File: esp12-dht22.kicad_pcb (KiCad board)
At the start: 2 copper layers, 42.9 x 18.5 mm, 12 parts, among them J1 Battery, U1 ESP-12E, U2 DHT22

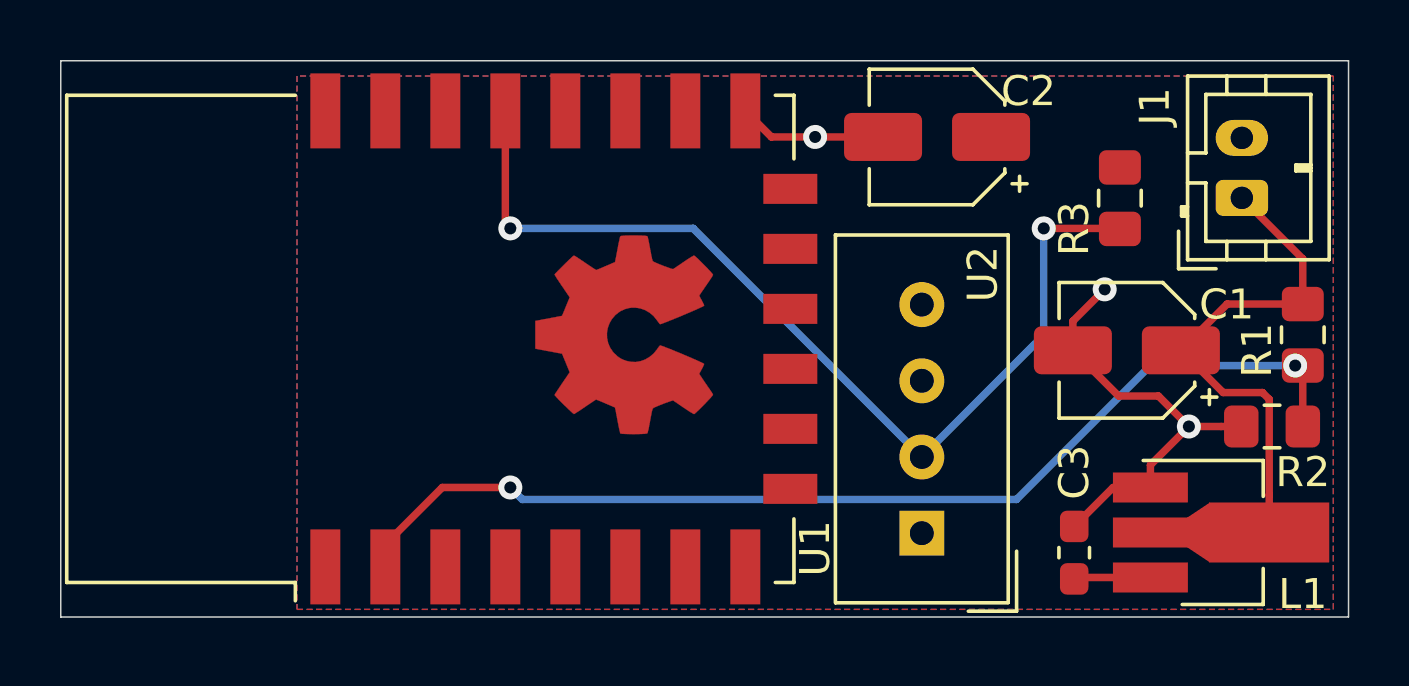
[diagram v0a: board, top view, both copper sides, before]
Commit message: added connection between RST and GPIO16 for wakeup from deep sleep fixes #1
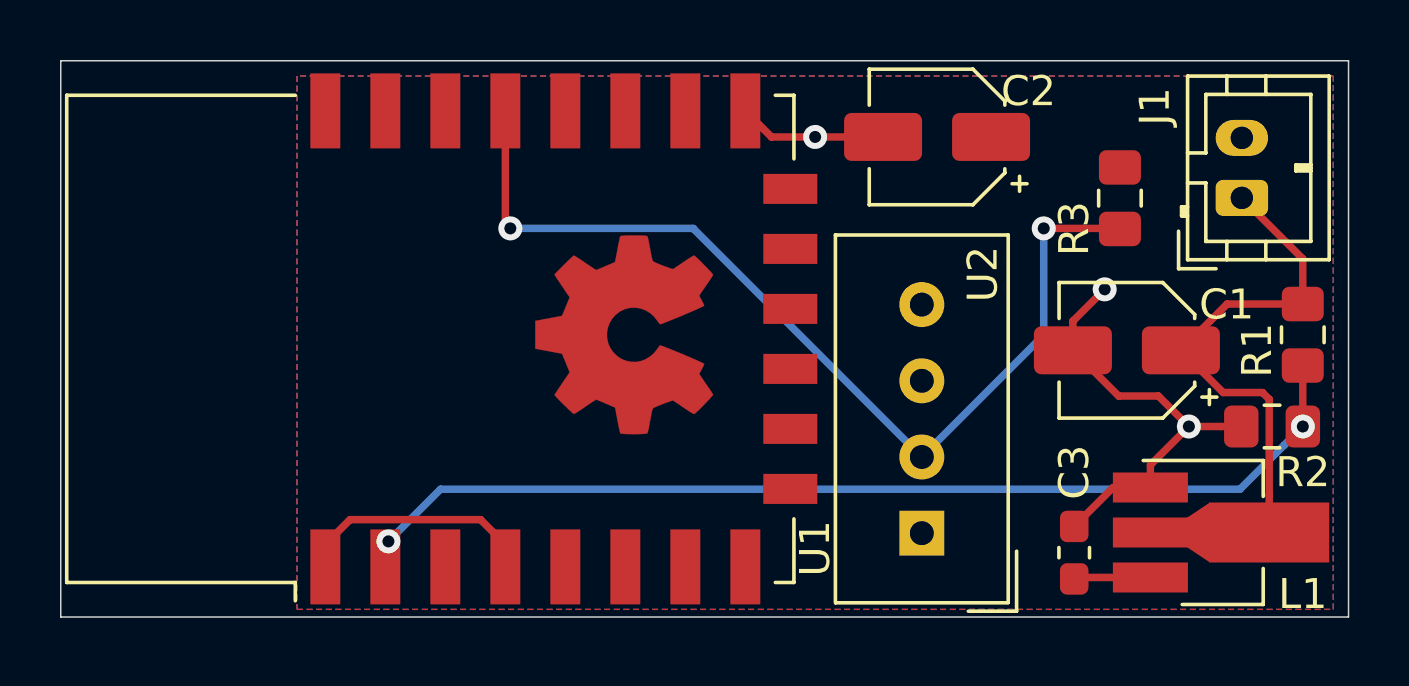
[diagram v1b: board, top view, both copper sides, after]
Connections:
- U1 pad 1: Net-(U1-Pad1) -> DeepSleep
- U1 pad 4: Net-(U1-Pad4) -> DeepSleep
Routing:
- net DeepSleep: track 0.00 -> 8.18 mm
- net ADC: track 36.2 -> 35.0 mm

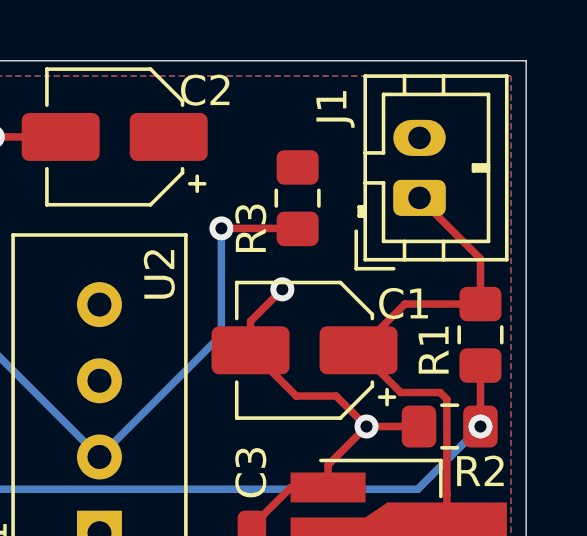
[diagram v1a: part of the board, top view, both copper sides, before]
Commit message: swapped pins of J1 fixes #4
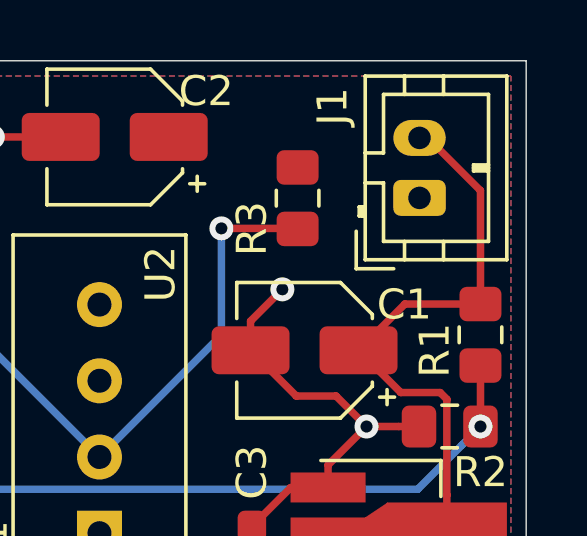
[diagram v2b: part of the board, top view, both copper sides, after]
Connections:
- J1 pad 1: +BATT -> GND
- J1 pad 2: GND -> +BATT
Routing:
- net +BATT: track 21.1 -> 23.3 mm
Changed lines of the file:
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@@
-(kicad_pcb (version 20171130) (host pcbnew 5.1.2-f72e74a~84~ubuntu18.10.1)
+(kicad_pcb (version 20171130) (host pcbnew 5.1.3-ffb9f22~84~ubuntu18.10.1)
   (general
     (thickness 1.6)
     (drawings 7)
-    (tracks 54)
+    (tracks 55)
     (zones 0)
     (modules 12)
@@
     )
     (pad 1 thru_hole roundrect (at 0 0 90) (size 1.2 1.75) (drill 0.75) (layers *.Cu *.Mask) (roundrect_rratio 0.208333)
+      (net 1 GND))
+    (pad 2 thru_hole oval (at 2 0 90) (size 1.2 1.75) (drill 0.75) (layers *.Cu *.Mask)
       (net 2 +BATT))
-    (pad 2 thru_hole oval (at 2 0 90) (size 1.2 1.75) (drill 0.75) (layers *.Cu *.Mask)
-      (net 1 GND))
     (model ${KISYS3DMOD}/Connector_JST.3dshapes/JST_PH_B2B-PH-K_1x02_P2.00mm_Vertical.wrl
       (at (xyz 0 0 0))
@@
   (segment (start 104.914 109.22) (end 105.93 110.236) (width 0.25) (layer F.Cu) (net 1))
   (segment (start 103.588 109.22) (end 104.914 109.22) (width 0.25) (layer F.Cu) (net 1))
-  (segment (start 109.728 104.648) (end 109.728 106.154) (width 0.25) (layer F.Cu) (net 2) (status 20))
-  (segment (start 107.696 102.616) (end 109.728 104.648) (width 0.25) (layer F.Cu) (net 2) (status 10))
   (segment (start 107.206 106.154) (end 105.664 107.696) (width 0.25) (layer F.Cu) (net 2) (status 20))
   (segment (start 109.728 106.154) (end 107.206 106.154) (width 0.25) (layer F.Cu) (net 2) (status 10))
@@
   (segment (start 106.148 113.768) (end 108.608 113.768) (width 0.25) (layer F.Cu) (net 2) (status 30))
   (segment (start 104.648 113.768) (end 106.148 113.768) (width 0.25) (layer F.Cu) (net 2) (status 30))
+  (segment (start 107.971 100.616) (end 107.696 100.616) (width 0.25) (layer F.Cu) (net 2))
+  (segment (start 109.728 106.154) (end 109.728 102.373) (width 0.25) (layer F.Cu) (net 2))
+  (segment (start 109.728 102.373) (end 107.971 100.616) (width 0.25) (layer F.Cu) (net 2))
   (segment (start 102.156 115.268) (end 102.108 115.316) (width 0.25) (layer F.Cu) (net 3) (status 30))
   (segment (start 104.648 115.268) (end 102.156 115.268) (width 0.25) (layer F.Cu) (net 3) (status 30))
-  (segment (start 109.728 108.204) (end 109.728 110.236) (width 0.25) (layer F.Cu) (net 4))
-  (via (at 109.728 110.236) (size 0.8) (drill 0.4) (layers F.Cu B.Cu) (net 4))
-  (via (at 79.248 114.064999) (size 0.8) (drill 0.4) (layers F.Cu B.Cu) (net 4))
-  (segment (start 79.145 114.915) (end 79.145 114.167999) (width 0.25) (layer F.Cu) (net 4))
-  (segment (start 79.145 114.167999) (end 79.248 114.064999) (width 0.25) (layer F.Cu) (net 4))
+  (segment (start 109.728 108.204) (end 109.728 110.236) (width 0.25) (layer F.Cu) (net 4) (status 30))
+  (via (at 109.728 110.236) (size 0.8) (drill 0.4) (layers F.Cu B.Cu) (net 4) (status 30))
+  (via (at 79.248 114.064999) (size 0.8) (drill 0.4) (layers F.Cu B.Cu) (net 4) (status 30))
+  (segment (start 79.145 114.915) (end 79.145 114.167999) (width 0.25) (layer F.Cu) (net 4) (status 30))
+  (segment (start 79.145 114.167999) (end 79.248 114.064999) (width 0.25) (layer F.Cu) (net 4) (status 30))
   (segment (start 109.104628 110.859372) (end 109.728 110.236) (width 0.25) (layer B.Cu) (net 4))
   (segment (start 107.636999 112.327001) (end 109.104628 110.859372) (width 0.25) (layer B.Cu) (net 4))
@@
   (segment (start 89.408 103.632) (end 97.028 111.252) (width 0.25) (layer B.Cu) (net 5) (status 20))
   (segment (start 83.312 103.632) (end 89.408 103.632) (width 0.25) (layer B.Cu) (net 5))
-  (segment (start 83.145 114.165) (end 83.145 114.915) (width 0.25) (layer F.Cu) (net 23))
-  (segment (start 82.319999 113.339999) (end 83.145 114.165) (width 0.25) (layer F.Cu) (net 23))
+  (segment (start 83.145 114.165) (end 83.145 114.915) (width 0.25) (layer F.Cu) (net 23) (status 30))
+  (segment (start 82.319999 113.339999) (end 83.145 114.165) (width 0.25) (layer F.Cu) (net 23) (status 20))
   (segment (start 77.970001 113.339999) (end 82.319999 113.339999) (width 0.25) (layer F.Cu) (net 23))
-  (segment (start 77.145 114.165) (end 77.970001 113.339999) (width 0.25) (layer F.Cu) (net 23))
-  (segment (start 77.145 114.915) (end 77.145 114.165) (width 0.25) (layer F.Cu) (net 23))
+  (segment (start 77.145 114.165) (end 77.970001 113.339999) (width 0.25) (layer F.Cu) (net 23) (status 10))
+  (segment (start 77.145 114.915) (end 77.145 114.165) (width 0.25) (layer F.Cu) (net 23) (status 30))
   (zone (net 1) (net_name GND) (layer B.Cu) (hatch edge 0.508)
     (connect_pads (clearance 0.508))

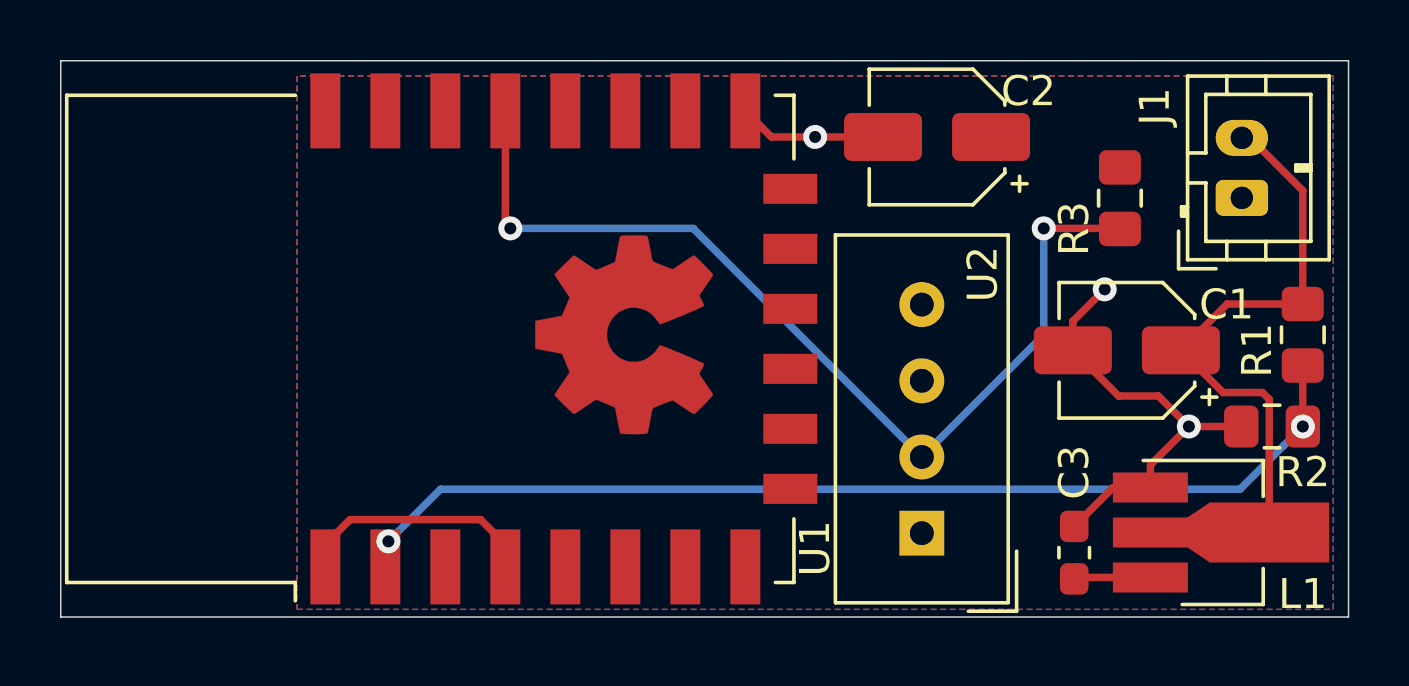
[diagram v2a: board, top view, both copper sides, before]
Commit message: connected ENABLE and GPIO15 to boot properly fixes #2
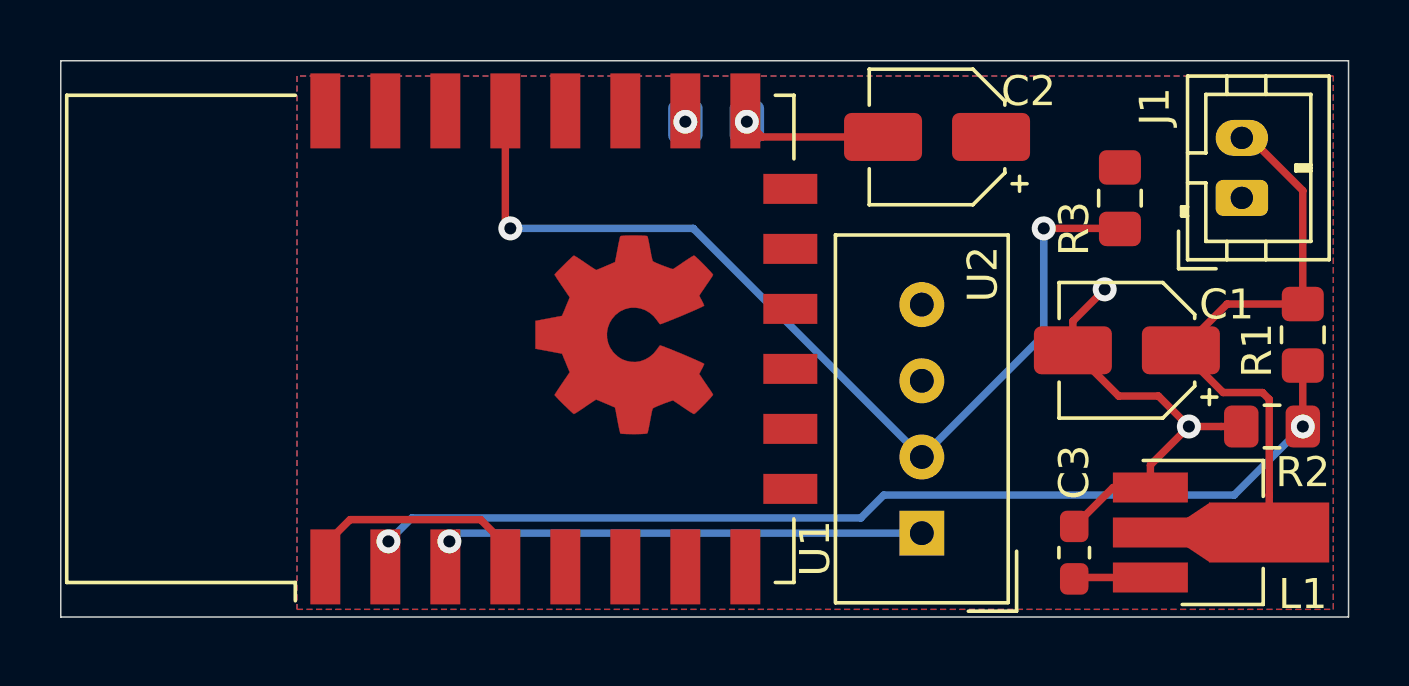
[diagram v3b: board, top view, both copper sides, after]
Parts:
- added R4: 2k2, Resistor_SMD:R_0805_2012Metric_Pad1.15x1.40mm_HandSolder, B.Cu at (90.2, 100.1)
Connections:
- U1 pad 3: Net-(U1-Pad3) -> VCC
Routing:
- net VCC: track 2.56 -> 19.3 mm, vias 0 -> 1
- net Net-(R4-Pad1): vias 0 -> 1

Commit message: connected DHT22 to Vbatt fixes #3
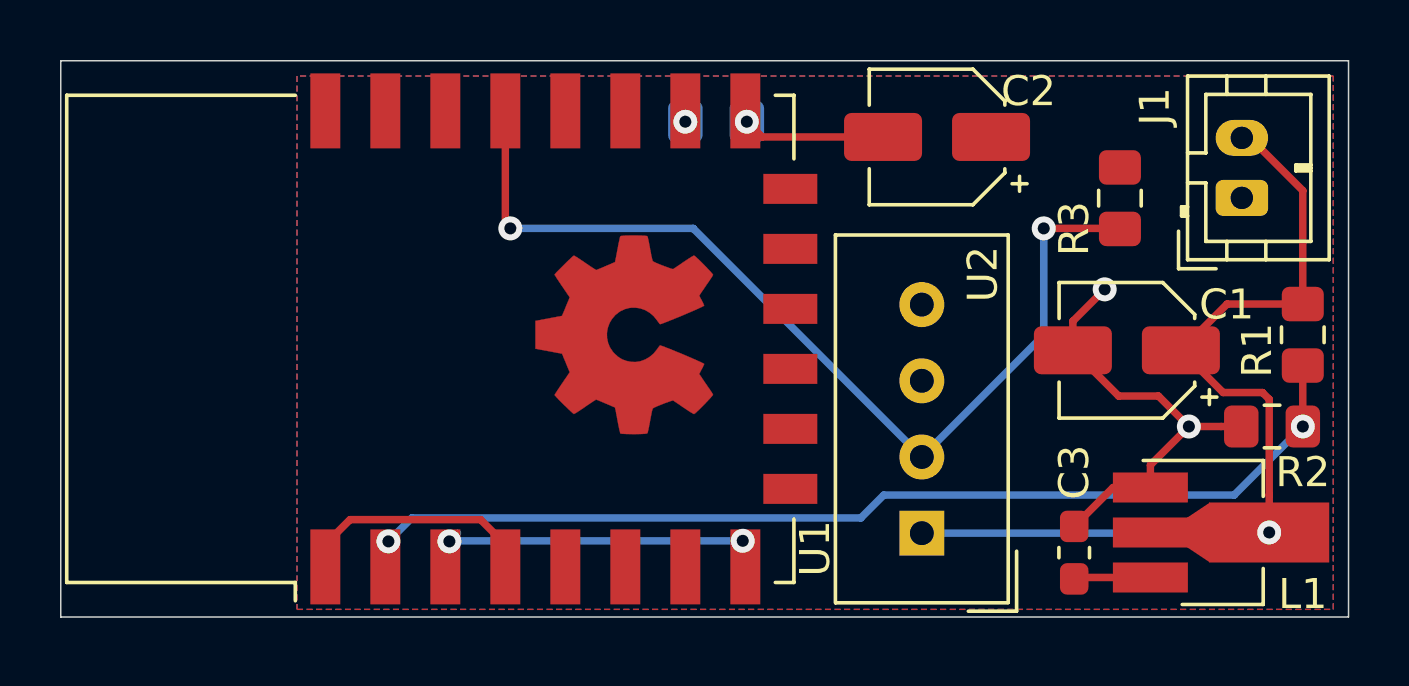
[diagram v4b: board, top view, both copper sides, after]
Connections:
- U2 pad 1: VCC -> +BATT
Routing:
- net +BATT: track 23.3 -> 34.9 mm, vias 0 -> 1
- net VCC: track 19.3 -> 14.5 mm, vias 1 -> 2
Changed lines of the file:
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@@
-(kicad_pcb (version 20171130) (host pcbnew 5.1.3-ffb9f22~84~ubuntu18.10.1)
+(kicad_pcb (version 20171130) (host pcbnew 5.1.5-52549c5~86~ubuntu19.10.1)
   (general
     (thickness 1.6)
     (drawings 7)
-    (tracks 61)
+    (tracks 68)
     (zones 0)
     (modules 13)
@@
     (fp_line (start -3.16 -2.6) (end -1.55 -2.6) (layer F.SilkS) (width 0.12))
     (pad 1 thru_hole rect (at 0 0 180) (size 1.5 1.5) (drill 0.8) (layers *.Cu *.Mask)
-      (net 3 VCC))
+      (net 2 +BATT))
     (pad 2 thru_hole circle (at 0 2.54 180) (size 1.5 1.5) (drill 0.8) (layers *.Cu *.Mask)
       (net 5 DHT_Data))
@@
   (segment (start 104.914 109.22) (end 105.93 110.236) (width 0.25) (layer F.Cu) (net 1))
   (segment (start 103.588 109.22) (end 104.914 109.22) (width 0.25) (layer F.Cu) (net 1))
-  (via (at 91.195 100.076) (size 0.8) (drill 0.4) (layers F.Cu B.Cu) (net 1))
-  (segment (start 91.703 100.584) (end 91.195 100.076) (width 0.25) (layer F.Cu) (net 1))
-  (segment (start 95.736 100.584) (end 91.703 100.584) (width 0.25) (layer F.Cu) (net 1))
+  (via (at 91.195 100.076) (size 0.8) (drill 0.4) (layers F.Cu B.Cu) (net 1) (status 30))
+  (segment (start 91.703 100.584) (end 91.195 100.076) (width 0.25) (layer F.Cu) (net 1) (status 20))
+  (segment (start 95.736 100.584) (end 91.703 100.584) (width 0.25) (layer F.Cu) (net 1) (status 10))
   (segment (start 107.206 106.154) (end 105.664 107.696) (width 0.25) (layer F.Cu) (net 2) (status 20))
   (segment (start 109.728 106.154) (end 107.206 106.154) (width 0.25) (layer F.Cu) (net 2) (status 10))
@@
   (segment (start 109.728 106.154) (end 109.728 102.373) (width 0.25) (layer F.Cu) (net 2) (status 10))
   (segment (start 109.728 102.373) (end 107.971 100.616) (width 0.25) (layer F.Cu) (net 2) (status 20))
+  (via (at 108.608 113.768) (size 0.8) (drill 0.4) (layers F.Cu B.Cu) (net 2))
+  (segment (start 108.584 113.792) (end 108.608 113.768) (width 0.25) (layer B.Cu) (net 2))
+  (segment (start 97.028 113.792) (end 108.584 113.792) (width 0.25) (layer B.Cu) (net 2))
   (segment (start 102.156 115.268) (end 102.108 115.316) (width 0.25) (layer F.Cu) (net 3) (status 30))
   (segment (start 104.648 115.268) (end 102.156 115.268) (width 0.25) (layer F.Cu) (net 3) (status 30))
-  (via (at 81.28 114.064999) (size 0.8) (drill 0.4) (layers F.Cu B.Cu) (net 3))
-  (segment (start 97.028 113.792) (end 81.552999 113.792) (width 0.25) (layer B.Cu) (net 3))
+  (via (at 81.28 114.064999) (size 0.8) (drill 0.4) (layers F.Cu B.Cu) (net 3) (status 30))
   (segment (start 81.552999 113.792) (end 81.28 114.064999) (width 0.25) (layer B.Cu) (net 3))
-  (segment (start 81.28 114.78) (end 81.145 114.915) (width 0.25) (layer F.Cu) (net 3))
-  (segment (start 81.28 114.064999) (end 81.28 114.78) (width 0.25) (layer F.Cu) (net 3))
+  (segment (start 81.28 114.78) (end 81.145 114.915) (width 0.25) (layer F.Cu) (net 3) (status 30))
+  (segment (start 81.28 114.064999) (end 81.28 114.78) (width 0.25) (layer F.Cu) (net 3) (status 30))
+  (via (at 91.059 114.046) (size 0.8) (drill 0.4) (layers F.Cu B.Cu) (net 3))
+  (segment (start 91.145 114.915) (end 91.145 114.132) (width 0.25) (layer F.Cu) (net 3))
+  (segment (start 91.145 114.132) (end 91.059 114.046) (width 0.25) (layer F.Cu) (net 3))
+  (segment (start 81.298999 114.046) (end 81.28 114.064999) (width 0.25) (layer B.Cu) (net 3))
+  (segment (start 91.059 114.046) (end 81.298999 114.046) (width 0.25) (layer B.Cu) (net 3))
   (via (at 109.728 110.236) (size 0.8) (drill 0.4) (layers F.Cu B.Cu) (net 4) (status 30))
   (segment (start 109.728 108.204) (end 109.728 110.236) (width 0.25) (layer F.Cu) (net 4) (status 30))
@@
   (segment (start 77.145 114.165) (end 77.970001 113.339999) (width 0.25) (layer F.Cu) (net 21) (status 10))
   (segment (start 77.145 114.915) (end 77.145 114.165) (width 0.25) (layer F.Cu) (net 21) (status 30))
-  (via (at 89.145 100.076) (size 0.8) (drill 0.4) (layers F.Cu B.Cu) (net 22))
+  (via (at 89.145 100.076) (size 0.8) (drill 0.4) (layers F.Cu B.Cu) (net 22) (status 30))
   (zone (net 1) (net_name GND) (layer B.Cu) (hatch edge 0.508)
     (connect_pads (clearance 0.508))
